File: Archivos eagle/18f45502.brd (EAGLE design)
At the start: 87.6 x 53 mm, 27 parts, among them IC1 PIC18F4550_40, IC2 7805DT, Q1 20MHz, X2 PN61729-S

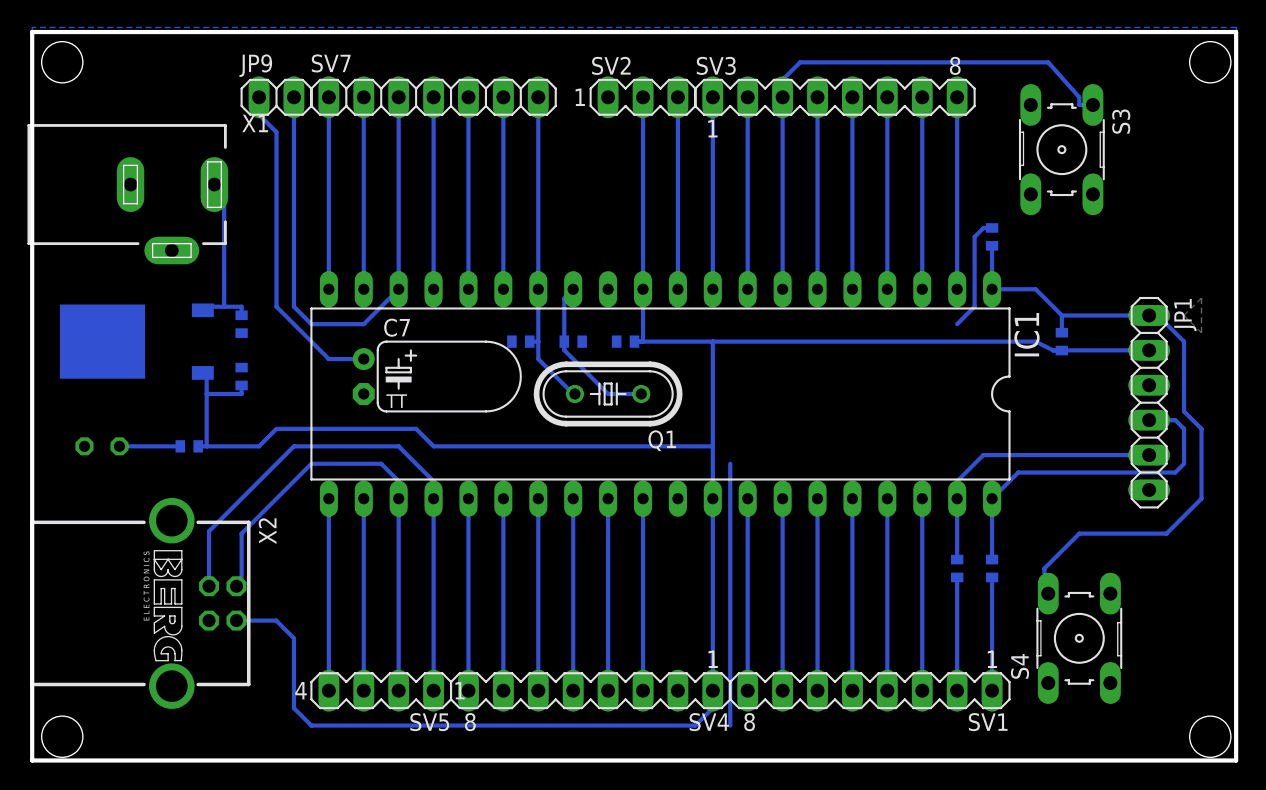
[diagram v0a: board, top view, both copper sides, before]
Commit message: build alpha 1.3
se acomodaron los agujeros porque estaban tocando el borde de la placa y
los pulsadores se re ubicaron de una forma simetrica
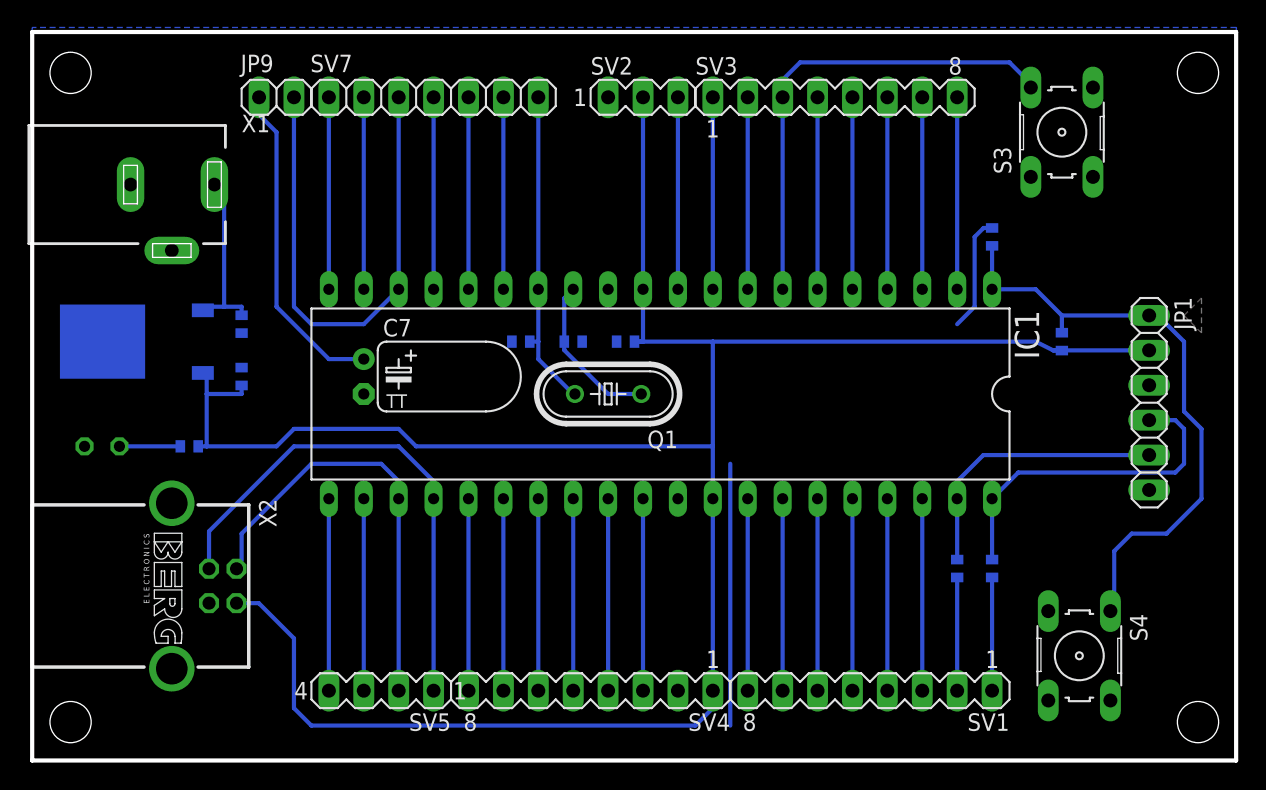
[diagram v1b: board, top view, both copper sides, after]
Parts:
- moved S4 1.27 mm to (76.2, 7.62), turned to 270 degrees
- moved X2 1.27 mm to (10.2, 12.7)
- moved S3 1.27 mm to (74.9, 45.7), turned to 90 degrees
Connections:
- net MCLR: now also S4.1; no longer S4.2
- net N$18: now also S3.2; no longer S3.1
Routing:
- net N$18: track 40.0 -> 34.7 mm
- net MCLR: track 47.7 -> 44.3 mm
- net D-: track 33.3 -> 32.0 mm
- net D+: track 39.2 -> 37.9 mm
- net VDD: track 171.8 -> 172.3 mm
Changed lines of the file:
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@@
 <wire x1="87.61" y1="53.01" x2="0" y2="53.01" width="0.3048" layer="20"/>
 <wire x1="0" y1="53.01" x2="0" y2="0" width="0.3048" layer="20"/>
-<hole x="2.19" y="50.81" drill="3"/>
-<hole x="2.19" y="1.73" drill="3"/>
-<hole x="85.73" y="50.81" drill="3"/>
-<hole x="85.73" y="1.73" drill="3"/>
+<hole x="2.794" y="50.038" drill="3"/>
+<hole x="2.794" y="2.794" drill="3"/>
+<hole x="84.836" y="50.038" drill="3"/>
+<hole x="84.836" y="2.794" drill="3"/>
 </plain>
 <attributes>
@@
 <element name="C5" library="resistor" package="C0402" value="22pF" x="39.37" y="30.48" rot="MR180"/>
 <element name="Q1" library="crystal" package="HC49/S" value="20MHz" x="41.91" y="26.67" rot="R180"/>
-<element name="X2" library="con-berg" package="PN61729-S" value="PN61729-S" x="10.16" y="11.43" rot="R270">
-<attribute name="MF" value="" x="10.16" y="11.43" size="1.778" layer="27" rot="R270" display="off"/>
-<attribute name="MPN" value="" x="10.16" y="11.43" size="1.778" layer="27" rot="R270" display="off"/>
-<attribute name="OC_FARNELL" value="unknown" x="10.16" y="11.43" size="1.778" layer="27" rot="R270" display="off"/>
-<attribute name="OC_NEWARK" value="unknown" x="10.16" y="11.43" size="1.778" layer="27" rot="R270" display="off"/>
+<element name="X2" library="con-berg" package="PN61729-S" value="PN61729-S" x="10.16" y="12.7" rot="R270">
+<attribute name="MF" value="" x="10.16" y="12.7" size="1.778" layer="27" rot="R270" display="off"/>
+<attribute name="MPN" value="" x="10.16" y="12.7" size="1.778" layer="27" rot="R270" display="off"/>
+<attribute name="OC_FARNELL" value="unknown" x="10.16" y="12.7" size="1.778" layer="27" rot="R270" display="off"/>
+<attribute name="OC_NEWARK" value="unknown" x="10.16" y="12.7" size="1.778" layer="27" rot="R270" display="off"/>
 </element>
 <element name="C6" library="resistor" package="C0402" value="100n" x="43.18" y="30.48" rot="MR0"/>
@@
 <element name="LED1" library="led" package="LED3MM" value="" x="5.08" y="22.86" rot="MR0"/>
 <element name="R4" library="resistor" package="R0402" value="1k" x="11.43" y="22.86" rot="MR180"/>
-<element name="S3" library="switch-omron" package="B3F-10XX" value="" x="74.93" y="44.45" rot="R270">
-<attribute name="MF" value="" x="74.93" y="44.45" size="1.778" layer="27" rot="R270" display="off"/>
-<attribute name="MPN" value="B3F-1000" x="74.93" y="44.45" size="1.778" layer="27" rot="R270" display="off"/>
-<attribute name="OC_FARNELL" value="176432" x="74.93" y="44.45" size="1.778" layer="27" rot="R270" display="off"/>
-<attribute name="OC_NEWARK" value="36M3542" x="74.93" y="44.45" size="1.778" layer="27" rot="R270" display="off"/>
-</element>
-<element name="S4" library="switch-omron" package="B3F-10XX" value="" x="76.2" y="8.89" rot="R90">
-<attribute name="MF" value="" x="76.2" y="8.89" size="1.778" layer="27" rot="R90" display="off"/>
-<attribute name="MPN" value="B3F-1000" x="76.2" y="8.89" size="1.778" layer="27" rot="R90" display="off"/>
-<attribute name="OC_FARNELL" value="176432" x="76.2" y="8.89" size="1.778" layer="27" rot="R90" display="off"/>
-<attribute name="OC_NEWARK" value="36M3542" x="76.2" y="8.89" size="1.778" layer="27" rot="R90" display="off"/>
+<element name="S3" library="switch-omron" package="B3F-10XX" value="" x="74.93" y="45.72" rot="R90">
+<attribute name="MF" value="" x="74.93" y="45.72" size="1.778" layer="27" rot="R90" display="off"/>
+<attribute name="MPN" value="B3F-1000" x="74.93" y="45.72" size="1.778" layer="27" rot="R90" display="off"/>
+<attribute name="OC_FARNELL" value="176432" x="74.93" y="45.72" size="1.778" layer="27" rot="R90" display="off"/>
+<attribute name="OC_NEWARK" value="36M3542" x="74.93" y="45.72" size="1.778" layer="27" rot="R90" display="off"/>
+</element>
+<element name="S4" library="switch-omron" package="B3F-10XX" value="" x="76.2" y="7.62" rot="R270">
+<attribute name="MF" value="" x="76.2" y="7.62" size="1.778" layer="27" rot="R270" display="off"/>
+<attribute name="MPN" value="B3F-1000" x="76.2" y="7.62" size="1.778" layer="27" rot="R270" display="off"/>
+<attribute name="OC_FARNELL" value="176432" x="76.2" y="7.62" size="1.778" layer="27" rot="R270" display="off"/>
+<attribute name="OC_NEWARK" value="36M3542" x="76.2" y="7.62" size="1.778" layer="27" rot="R270" display="off"/>
 </element>
 <element name="IC2" library="linear" package="TO252" value="7805DT" x="7.62" y="30.48" rot="MR270"/>
@@
 <wire x1="49.53" y1="5.08" x2="49.53" y2="19.05" width="0.3048" layer="16"/>
 <wire x1="44.45" y1="34.29" x2="44.45" y2="48.26" width="0.3048" layer="16"/>
-<wire x1="17.76" y1="10.18" x2="14.87" y2="10.18" width="0.3048" layer="16"/>
-<wire x1="19.05" y1="8.89" x2="17.76" y2="10.18" width="0.3048" layer="16"/>
+<wire x1="16.49" y1="11.45" x2="14.87" y2="11.45" width="0.3048" layer="16"/>
+<wire x1="19.05" y1="8.89" x2="16.49" y2="11.45" width="0.3048" layer="16"/>
 <wire x1="19.05" y1="3.81" x2="19.05" y2="8.89" width="0.3048" layer="16"/>
 <wire x1="20.32" y1="2.54" x2="19.05" y2="3.81" width="0.3048" layer="16"/>
@@
 <wire x1="12.08" y1="22.86" x2="12.7" y2="22.86" width="0.3048" layer="16"/>
 <wire x1="12.7" y1="22.86" x2="12.7" y2="26.67" width="0.3048" layer="16"/>
-<wire x1="12.7" y1="22.86" x2="16.51" y2="22.86" width="0.3048" layer="16"/>
-<wire x1="16.51" y1="22.86" x2="17.78" y2="24.13" width="0.3048" layer="16"/>
-<wire x1="17.78" y1="24.13" x2="27.94" y2="24.13" width="0.3048" layer="16"/>
-<wire x1="27.94" y1="24.13" x2="29.21" y2="22.86" width="0.3048" layer="16"/>
-<wire x1="29.21" y1="22.86" x2="49.53" y2="22.86" width="0.3048" layer="16"/>
+<wire x1="12.7" y1="22.86" x2="17.78" y2="22.86" width="0.3048" layer="16"/>
+<wire x1="17.78" y1="22.86" x2="19.05" y2="24.13" width="0.3048" layer="16"/>
+<wire x1="19.05" y1="24.13" x2="26.67" y2="24.13" width="0.3048" layer="16"/>
+<wire x1="26.67" y1="24.13" x2="27.94" y2="22.86" width="0.3048" layer="16"/>
+<wire x1="27.94" y1="22.86" x2="49.53" y2="22.86" width="0.3048" layer="16"/>
 </signal>
 <signal name="RB6">
@@
 <wire x1="19.05" y1="22.86" x2="26.67" y2="22.86" width="0.3048" layer="16"/>
 <wire x1="19.05" y1="22.86" x2="12.87" y2="16.68" width="0.3048" layer="16"/>
-<wire x1="12.87" y1="16.68" x2="12.87" y2="12.68" width="0.3048" layer="16"/>
+<wire x1="12.87" y1="16.68" x2="12.87" y2="13.95" width="0.3048" layer="16"/>
 </signal>
 <signal name="D-">
@@
 <wire x1="25.4" y1="21.59" x2="20.32" y2="21.59" width="0.3048" layer="16"/>
 <wire x1="20.32" y1="21.59" x2="15.24" y2="16.51" width="0.3048" layer="16"/>
-<wire x1="15.24" y1="16.51" x2="15.24" y2="13.05" width="0.3048" layer="16"/>
-<wire x1="15.24" y1="13.05" x2="14.87" y2="12.68" width="0.3048" layer="16"/>
+<wire x1="15.24" y1="16.51" x2="15.24" y2="14.32" width="0.3048" layer="16"/>
+<wire x1="15.24" y1="14.32" x2="14.87" y2="13.95" width="0.3048" layer="16"/>
 </signal>
 <signal name="N$46">
@@
 <contactref element="IC1" pad="1"/>
 <contactref element="JP1" pad="1"/>
-<contactref element="S4" pad="2"/>
 <wire x1="69.85" y1="34.29" x2="69.85" y2="37.45" width="0.3048" layer="16"/>
 <wire x1="81.28" y1="32.385" x2="74.93" y2="32.385" width="0.3048" layer="16"/>
@@
 <wire x1="81.915" y1="32.385" x2="81.28" y2="32.385" width="0.3048" layer="16"/>
 <wire x1="83.82" y1="30.48" x2="81.915" y2="32.385" width="0.3048" layer="16"/>
-<wire x1="73.9394" y1="12.1412" x2="74.2188" y2="11.9888" width="0.3048" layer="16"/>
 <wire x1="85.09" y1="24.13" x2="85.09" y2="19.05" width="0.3048" layer="16"/>
 <wire x1="85.09" y1="19.05" x2="82.55" y2="16.51" width="0.3048" layer="16"/>
-<wire x1="82.55" y1="16.51" x2="76.2" y2="16.51" width="0.3048" layer="16"/>
-<wire x1="76.2" y1="16.51" x2="73.66" y2="13.97" width="0.3048" layer="16"/>
-<wire x1="73.66" y1="13.97" x2="73.66" y2="12.7" width="0.3048" layer="16"/>
-<wire x1="73.66" y1="12.7" x2="73.9394" y2="12.1412" width="0.3048" layer="16"/>
+<contactref element="S4" pad="1"/>
+<wire x1="82.55" y1="16.51" x2="80.01" y2="16.51" width="0.3048" layer="16"/>
+<wire x1="80.01" y1="16.51" x2="78.74" y2="15.24" width="0.3048" layer="16"/>
+<wire x1="78.74" y1="15.24" x2="78.74" y2="11.1506" width="0.3048" layer="16"/>
+<wire x1="78.74" y1="11.1506" x2="78.4606" y2="10.8712" width="0.3048" layer="16"/>
 </signal>
 <signal name="GND">
@@
 <contactref element="C1" pad="2"/>
 <contactref element="IC2" pad="3"/>
-<wire x1="46.99" y1="5.08" x2="50.8" y2="2.54" width="0" layer="19" extent="16-16"/>
+<wire x1="50.8" y1="2.54" x2="46.99" y2="5.08" width="0" layer="19" extent="16-16"/>
 </signal>
 <signal name="N$3">
@@
 <contactref element="IC1" pad="7"/>
 <contactref element="SV3" pad="3"/>
-<contactref element="S3" pad="1"/>
 <wire x1="54.61" y1="34.29" x2="54.61" y2="48.26" width="0.3048" layer="16"/>
-<wire x1="55.88" y1="50.8" x2="73.9394" y2="50.8" width="0.3048" layer="16"/>
-<wire x1="73.9394" y1="50.8" x2="76.2" y2="48.26" width="0.3048" layer="16"/>
-<wire x1="76.2" y1="48.26" x2="76.2" y2="47.7012" width="0.3048" layer="16"/>
-<wire x1="76.2" y1="47.7012" x2="77.1906" y2="47.7012" width="0.3048" layer="16"/>
+<wire x1="55.88" y1="50.8" x2="71.12" y2="50.8" width="0.3048" layer="16"/>
 <wire x1="55.88" y1="50.8" x2="54.61" y2="49.53" width="0.3048" layer="16"/>
 <wire x1="54.61" y1="49.53" x2="54.61" y2="48.26" width="0.3048" layer="16"/>
+<contactref element="S3" pad="2"/>
+<wire x1="71.12" y1="50.8" x2="72.39" y2="49.53" width="0.3048" layer="16"/>
+<wire x1="72.39" y1="49.53" x2="72.6694" y2="48.9712" width="0.3048" layer="16"/>
 </signal>
 <signal name="N$19">

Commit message: build alpha 1.3.1
modificaciones menores
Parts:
- moved S3 1.27 mm to (76.2, 45.7)
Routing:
- net N$18: track 34.7 -> 36.0 mm
- net VDD: track 172.3 -> 171.8 mm
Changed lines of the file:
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@@
 <element name="LED1" library="led" package="LED3MM" value="" x="5.08" y="22.86" rot="MR0"/>
 <element name="R4" library="resistor" package="R0402" value="1k" x="11.43" y="22.86" rot="MR180"/>
-<element name="S3" library="switch-omron" package="B3F-10XX" value="" x="74.93" y="45.72" rot="R90">
-<attribute name="MF" value="" x="74.93" y="45.72" size="1.778" layer="27" rot="R90" display="off"/>
-<attribute name="MPN" value="B3F-1000" x="74.93" y="45.72" size="1.778" layer="27" rot="R90" display="off"/>
-<attribute name="OC_FARNELL" value="176432" x="74.93" y="45.72" size="1.778" layer="27" rot="R90" display="off"/>
-<attribute name="OC_NEWARK" value="36M3542" x="74.93" y="45.72" size="1.778" layer="27" rot="R90" display="off"/>
+<element name="S3" library="switch-omron" package="B3F-10XX" value="" x="76.2" y="45.72" rot="R90">
+<attribute name="MF" value="" x="76.2" y="45.72" size="1.778" layer="27" rot="R90" display="off"/>
+<attribute name="MPN" value="B3F-1000" x="76.2" y="45.72" size="1.778" layer="27" rot="R90" display="off"/>
+<attribute name="OC_FARNELL" value="176432" x="76.2" y="45.72" size="1.778" layer="27" rot="R90" display="off"/>
+<attribute name="OC_NEWARK" value="36M3542" x="76.2" y="45.72" size="1.778" layer="27" rot="R90" display="off"/>
 </element>
 <element name="S4" library="switch-omron" package="B3F-10XX" value="" x="76.2" y="7.62" rot="R270">
@@
 <wire x1="44.45" y1="30.48" x2="44.45" y2="34.29" width="0.3048" layer="16"/>
 <wire x1="44.45" y1="30.48" x2="43.83" y2="30.48" width="0.3048" layer="16"/>
-<wire x1="49.53" y1="19.05" x2="49.53" y2="22.86" width="0.3048" layer="16"/>
-<wire x1="49.53" y1="22.86" x2="49.53" y2="30.48" width="0.3048" layer="16"/>
+<wire x1="49.53" y1="19.05" x2="49.53" y2="24.13" width="0.3048" layer="16"/>
+<wire x1="49.53" y1="24.13" x2="49.53" y2="30.48" width="0.3048" layer="16"/>
 <wire x1="49.53" y1="30.48" x2="43.83" y2="30.48" width="0.3048" layer="16"/>
 <wire x1="49.53" y1="30.48" x2="73.025" y2="30.48" width="0.3048" layer="16"/>
@@
 <wire x1="12.7" y1="22.86" x2="17.78" y2="22.86" width="0.3048" layer="16"/>
 <wire x1="17.78" y1="22.86" x2="19.05" y2="24.13" width="0.3048" layer="16"/>
-<wire x1="19.05" y1="24.13" x2="26.67" y2="24.13" width="0.3048" layer="16"/>
-<wire x1="26.67" y1="24.13" x2="27.94" y2="22.86" width="0.3048" layer="16"/>
-<wire x1="27.94" y1="22.86" x2="49.53" y2="22.86" width="0.3048" layer="16"/>
+<wire x1="19.05" y1="24.13" x2="49.53" y2="24.13" width="0.3048" layer="16"/>
 </signal>
 <signal name="RB6">
+<contactref element="JP1" pad="5"/>
+<wire x1="69.215" y1="22.225" x2="81.28" y2="22.225" width="0.3048" layer="16"/>
+<wire x1="67.31" y1="20.32" x2="69.215" y2="22.225" width="0.3048" layer="16"/>
 <contactref element="IC1" pad="39"/>
 <contactref element="R1" pad="1"/>
-<contactref element="JP1" pad="5"/>
-<wire x1="67.31" y1="14.62" x2="67.31" y2="19.05" width="0.3048" layer="16"/>
-<wire x1="69.215" y1="22.225" x2="81.28" y2="22.225" width="0.3048" layer="16"/>
-<wire x1="67.31" y1="20.32" x2="69.215" y2="22.225" width="0.3048" layer="16"/>
+<wire x1="67.31" y1="19.05" x2="67.31" y2="14.62" width="0.3048" layer="16"/>
 <wire x1="67.31" y1="19.05" x2="67.31" y2="20.32" width="0.3048" layer="16"/>
 </signal>
@@
 </signal>
 <signal name="RB7">
-<contactref element="IC1" pad="40"/>
-<contactref element="R3" pad="1"/>
 <contactref element="JP1" pad="4"/>
-<wire x1="69.85" y1="14.62" x2="69.85" y2="19.05" width="0.3048" layer="16"/>
-<wire x1="69.85" y1="19.05" x2="71.755" y2="20.955" width="0.3048" layer="16"/>
 <wire x1="80.01" y1="24.765" x2="81.28" y2="24.765" width="0.3048" layer="16"/>
 <wire x1="71.755" y1="20.955" x2="83.185" y2="20.955" width="0.3048" layer="16"/>
@@
 <wire x1="83.82" y1="24.13" x2="83.185" y2="24.765" width="0.3048" layer="16"/>
 <wire x1="83.185" y1="24.765" x2="81.28" y2="24.765" width="0.3048" layer="16"/>
+<contactref element="R3" pad="1"/>
+<contactref element="IC1" pad="40"/>
+<wire x1="69.85" y1="19.05" x2="69.85" y2="14.62" width="0.3048" layer="16"/>
+<wire x1="69.85" y1="19.05" x2="71.755" y2="20.955" width="0.3048" layer="16"/>
 </signal>
 <signal name="OSC1">
@@
 <contactref element="IC1" pad="12"/>
 <contactref element="IC1" pad="31"/>
-<contactref element="X2" pad="4"/>
-<contactref element="C6" pad="2"/>
 <contactref element="C8" pad="2"/>
 <contactref element="C5" pad="2"/>
@@
 <contactref element="C1" pad="2"/>
 <contactref element="IC2" pad="3"/>
-<wire x1="50.8" y1="2.54" x2="46.99" y2="5.08" width="0" layer="19" extent="16-16"/>
+<contactref element="C6" pad="2"/>
+<contactref element="X2" pad="4"/>
+<wire x1="46.99" y1="5.08" x2="50.8" y2="2.54" width="0" layer="19" extent="16-16"/>
 </signal>
 <signal name="N$3">
@@
 <contactref element="SV3" pad="3"/>
 <wire x1="54.61" y1="34.29" x2="54.61" y2="48.26" width="0.3048" layer="16"/>
-<wire x1="55.88" y1="50.8" x2="71.12" y2="50.8" width="0.3048" layer="16"/>
+<wire x1="55.88" y1="50.8" x2="72.39" y2="50.8" width="0.3048" layer="16"/>
 <wire x1="55.88" y1="50.8" x2="54.61" y2="49.53" width="0.3048" layer="16"/>
 <wire x1="54.61" y1="49.53" x2="54.61" y2="48.26" width="0.3048" layer="16"/>
 <contactref element="S3" pad="2"/>
-<wire x1="71.12" y1="50.8" x2="72.39" y2="49.53" width="0.3048" layer="16"/>
-<wire x1="72.39" y1="49.53" x2="72.6694" y2="48.9712" width="0.3048" layer="16"/>
+<wire x1="72.39" y1="50.8" x2="73.66" y2="49.53" width="0.3048" layer="16"/>
+<wire x1="73.66" y1="49.53" x2="73.9394" y2="48.9712" width="0.3048" layer="16"/>
 </signal>
 <signal name="N$19">
@@
 </signal>
 </signals>
+<errors>
+</errors>
 </board>
 </drawing>

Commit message: build alpha 1.4
0402 por 0805
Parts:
- C1, C2, C4, C5, C6, C8: device resistor:C0402 -> resistor:C0805K
- R1, R2, R3, R4: device resistor:R0402 -> resistor:R0805
- moved C6 10.2 mm to (53.3, 29.2), turned to 270 degrees
- moved C5 1.27 mm to (40.6, 30.5)
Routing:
- net VDD: track 171.8 -> 169.5 mm
- net OSC1: track 11.6 -> 10.7 mm
- net MCLR: track 44.3 -> 43.8 mm
